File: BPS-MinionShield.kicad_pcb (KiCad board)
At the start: 2 copper layers, 85 x 66 mm, 83 parts, among them J1 TempConn1, J2 TempConn2, J3 Conn_01x24_Female

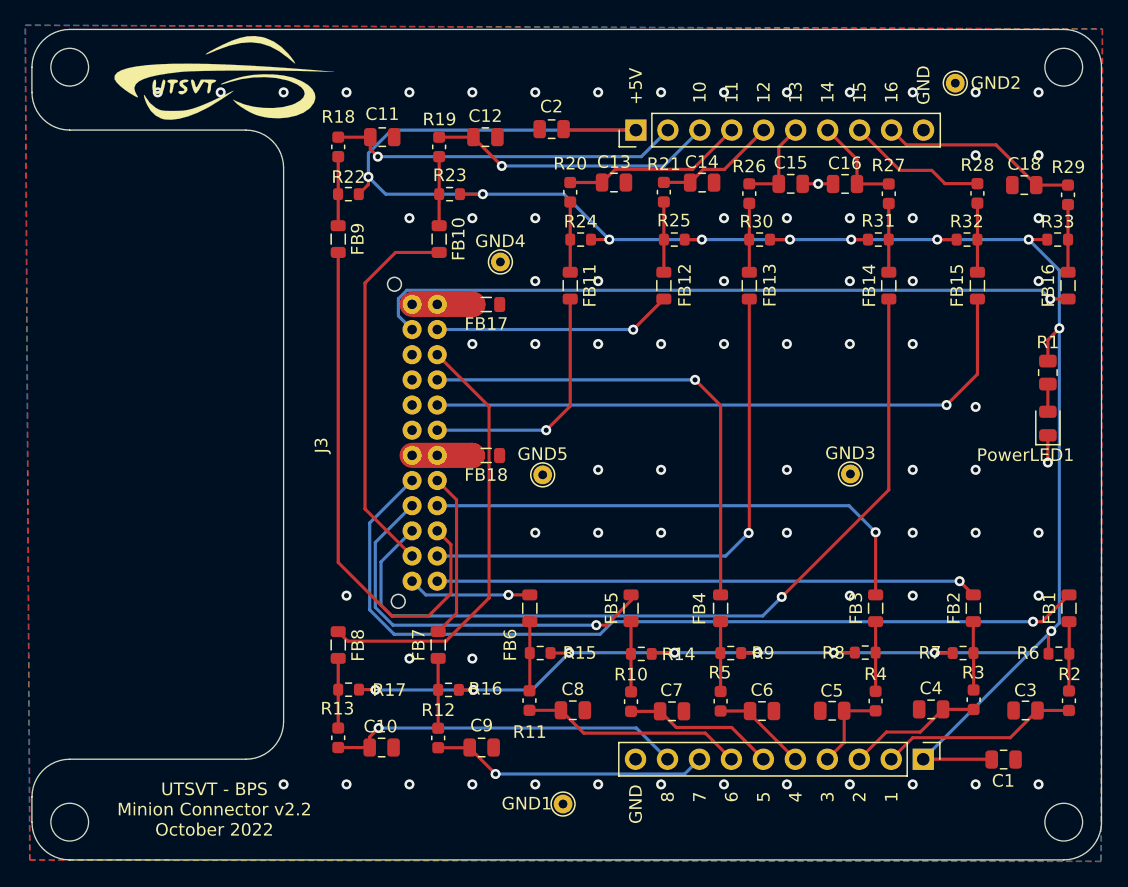
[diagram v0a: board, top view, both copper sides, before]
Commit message: removed some gnd test points
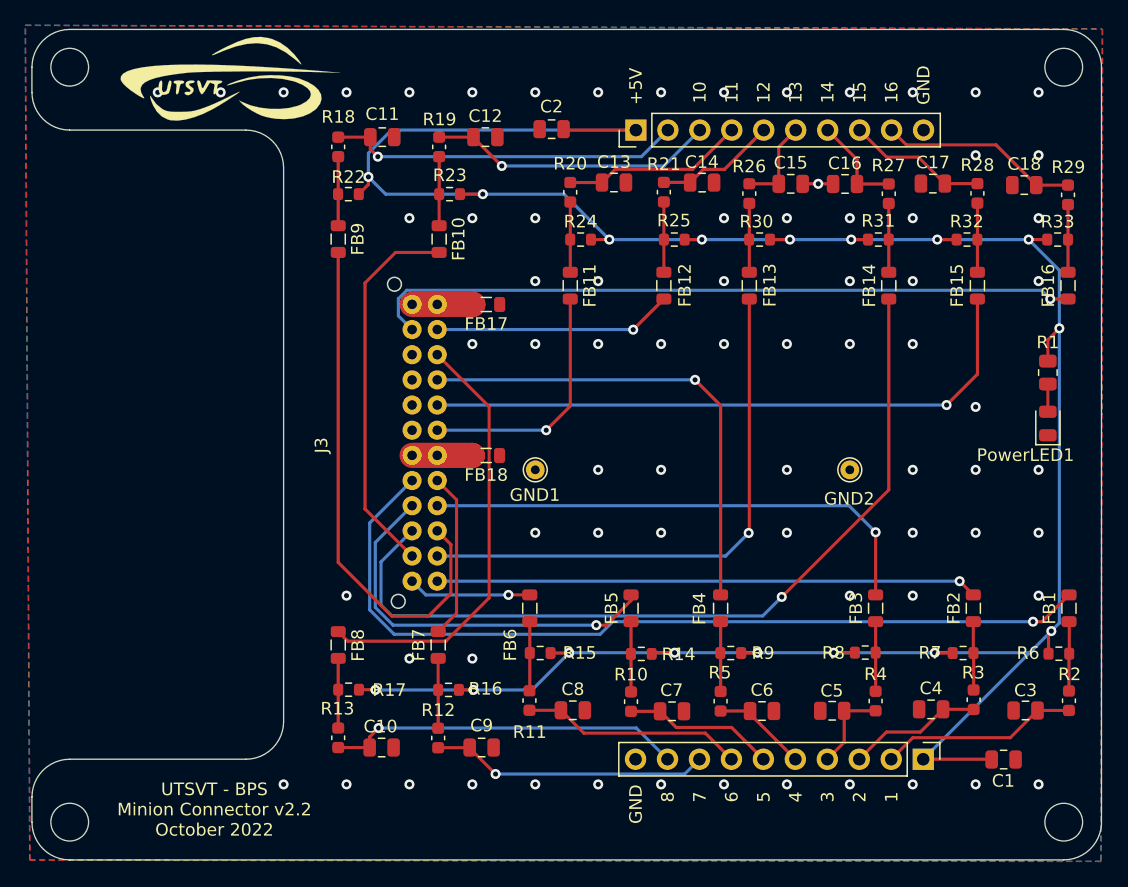
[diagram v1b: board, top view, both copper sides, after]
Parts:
- removed GND3, GND4, GND5: TestPoint, TestPoint:TestPoint_THTPad_D1.5mm_Drill0.7mm
- added C17: 1u, Capacitor_SMD:C_0805_2012Metric, F.Cu at (171.6, 82.2)
- moved GND2 31.9 mm to (165.0, 105.0), turned to 180 degrees
- moved GND1 26.7 mm to (140.0, 105.0), turned to 90 degrees
- moved G*** 0.49 mm to (127.9, 125.6)
- moved G*** 0.49 mm to (115.5, 74.1)
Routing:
- net GND: track 5.04 -> 2.88 mm

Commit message: implemented hannah changes and added personalization
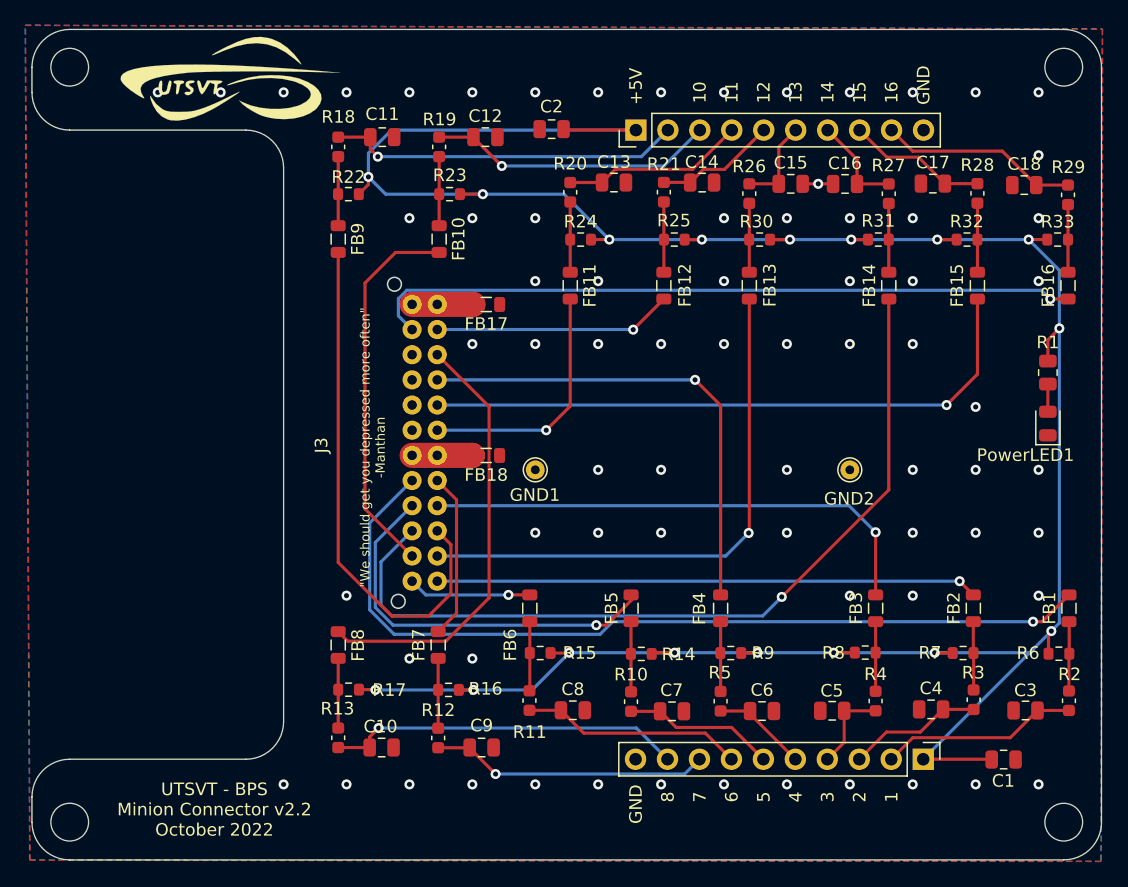
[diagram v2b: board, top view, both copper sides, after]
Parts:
- added G***: LOGO, LOGO, B.Cu at (156.2, 108.0)
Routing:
- net GND: vias 73 -> 72
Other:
- board text added: "{dblquote}We should get you depressed more often{dblquote} -Manthan"
- board text added: "{dblquote}You spent $10 on that haircut just to get no bitches?{dblquote} Tasnia Bari to Raymond Jiang"

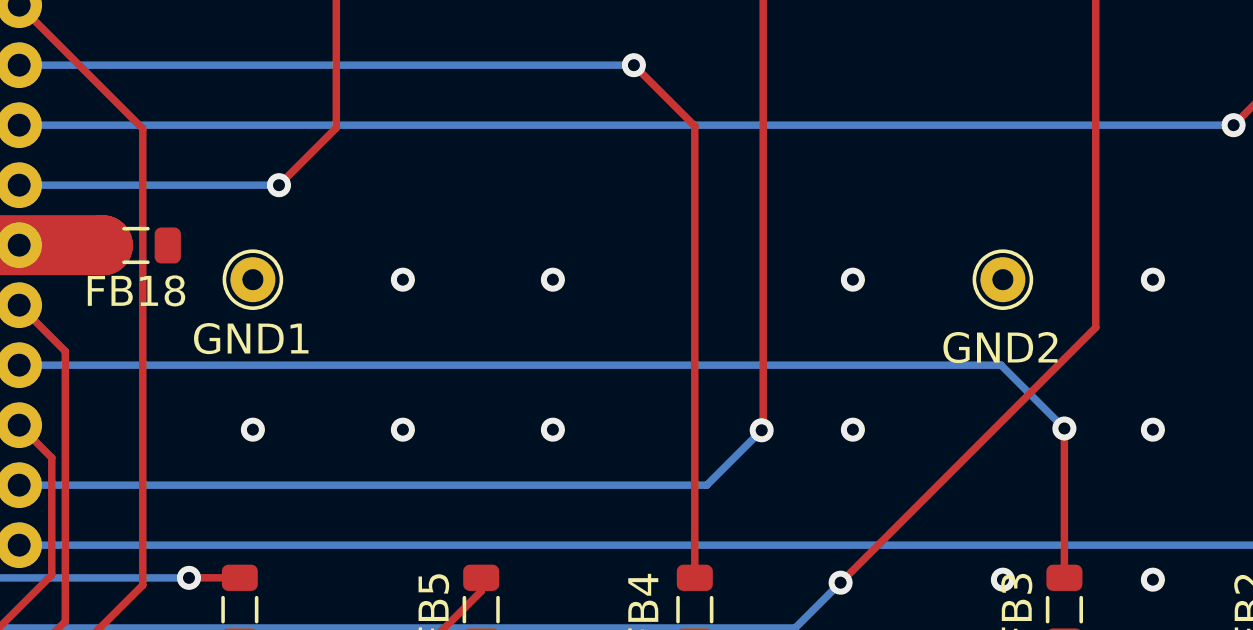
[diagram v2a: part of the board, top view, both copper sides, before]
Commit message: keep just 1 gnd testpoint
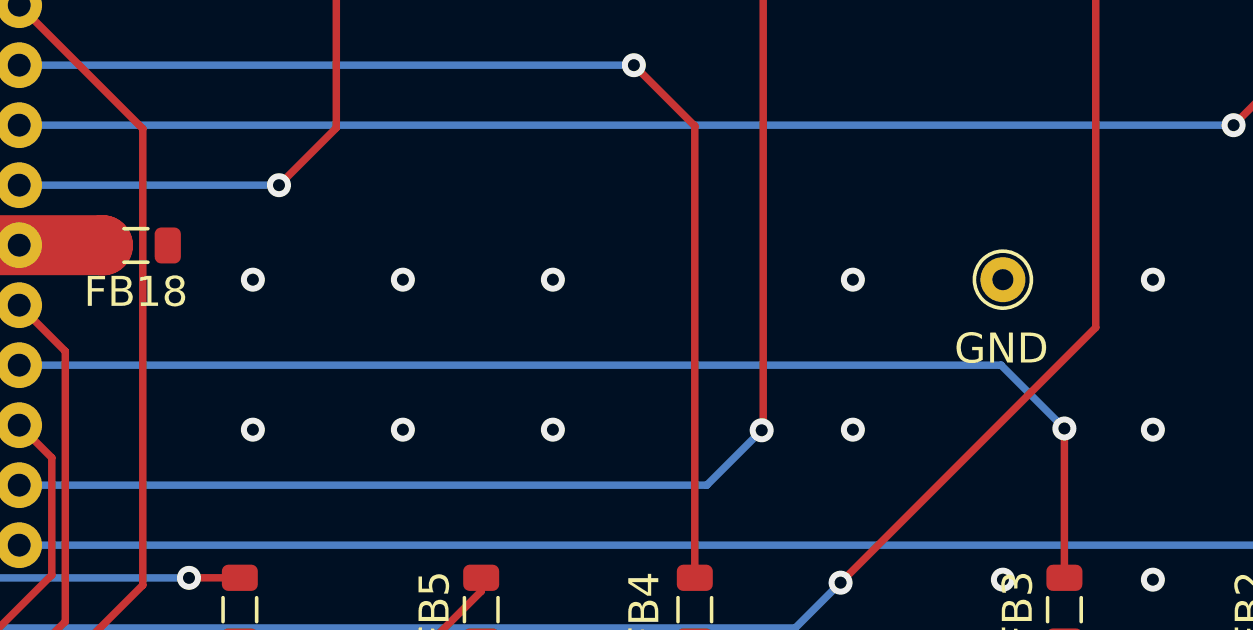
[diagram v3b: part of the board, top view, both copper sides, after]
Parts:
- removed GND1: TestPoint, TestPoint:TestPoint_THTPad_D1.5mm_Drill0.7mm
- renumbered GND2 to GND
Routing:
- net GND: vias 72 -> 73
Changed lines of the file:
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@@
     (property "Sheetname" "")
     (attr exclude_from_pos_files)
-    (fp_text reference "GND2" (at 0.05 -2.3 180) (layer "F.SilkS")
+    (fp_text reference "GND" (at 0.05 -2.3 180) (layer "F.SilkS")
       (effects (font (size 1 1) (thickness 0.15)))
     )
@@
     )
   )
-  (footprint "TestPoint:TestPoint_THTPad_D1.5mm_Drill0.7mm" (layer "F.Cu")
-    (at 140 105 90)
-    (descr "THT pad as test Point, diameter 1.5mm, hole diameter 0.7mm")
-    (tags "test point THT pad")
-    (property "Sheetfile" "BPS-MinionShield.kicad_sch")
-    (property "Sheetname" "")
-    (attr exclude_from_pos_files)
-    (fp_text reference "GND1" (at -2 -0.03 180) (layer "F.SilkS")
-      (effects (font (size 1 1) (thickness 0.15)))
-    )
-    (fp_text value "TestPoint" (at 0 1.75 90) (layer "F.Fab")
-      (effects (font (size 1 1) (thickness 0.15)))
-    )
-    (fp_text user "${REFERENCE}" (at 0 -1.65 90) (layer "F.Fab")
-      (effects (font (size 1 1) (thickness 0.15)))
-    )
-    (fp_circle (center 0 0) (end 0 0.95) (layer "F.SilkS") (width 0.12) (fill none))
-    (fp_circle (center 0 0) (end 1.25 0) (layer "F.CrtYd") (width 0.05) (fill none))
-    (pad "1" thru_hole circle (at 0 0 90) (size 1.5 1.5) (drill 0.7) (layers *.Cu *.Mask)
-      (net 2 "GND") (pinfunction "1") (pintype "passive"))
-  )
   (footprint "Capacitor_SMD:C_0805_2012Metric" (layer "F.Cu")
     (at 171.46 124.035)
@@
   (via (at 170 105) (size 0.8) (drill 0.4) (layers "F.Cu" "B.Cu") (free) (net 2))
   (via (at 140 90) (size 0.8) (drill 0.4) (layers "F.Cu" "B.Cu") (free) (net 2))
+  (via (at 140 105) (size 0.8) (drill 0.4) (layers "F.Cu" "B.Cu") (free) (net 2))
   (via (at 175 105) (size 0.8) (drill 0.4) (layers "F.Cu" "B.Cu") (free) (net 2))
   (via (at 145 110) (size 0.8) (drill 0.4) (layers "F.Cu" "B.Cu") (free) (net 2))

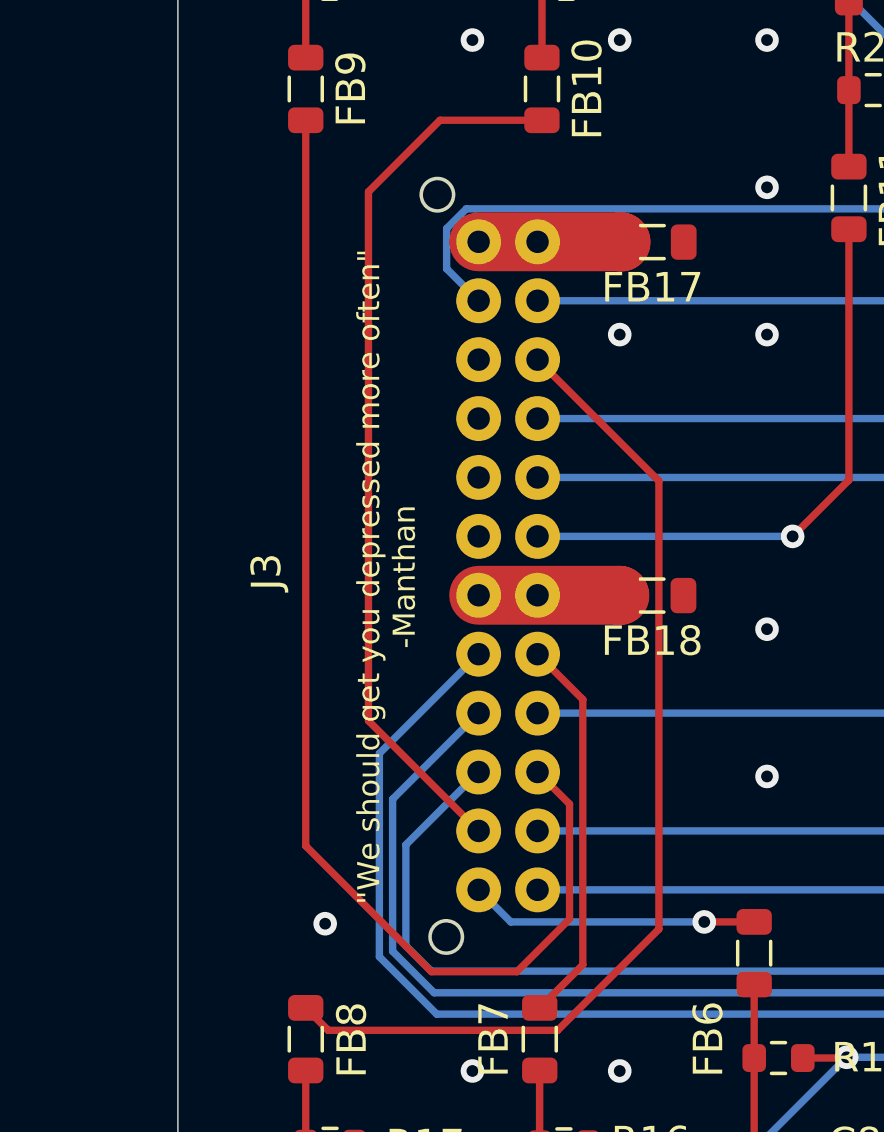
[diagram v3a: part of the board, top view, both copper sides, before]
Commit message: fix connector footprint, change quotes
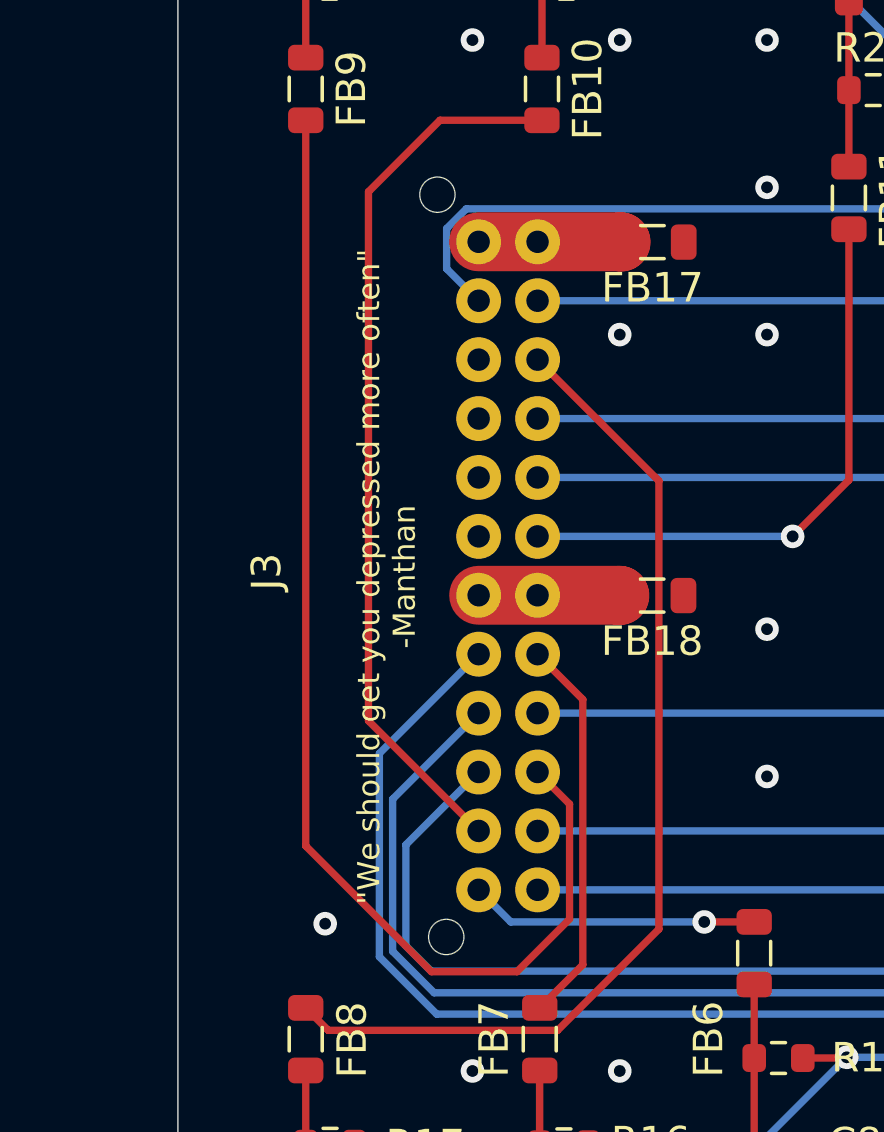
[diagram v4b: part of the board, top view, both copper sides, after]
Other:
- board text added: "Champers was here"
- board text added: "{dblquote}Too much lube is never a problem{dblquote} -Raymond Jiang"
- board text added: "{dblquote}git gud{dblquote} -Prof. Alex Hanson to 302 students during a midterm"
- board text removed: "Why you turn me over???"
- board text removed: "{dblquote}You spent $10 on that haircut just to get no bitches?{dblquote} Tasnia Bari to Raymond Jiang"
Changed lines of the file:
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@@
       (effects (font (size 1 1) (thickness 0.15)))
     )
-    (fp_circle (center 23.6 -1.4) (end 23.05 -1.4) (layer "Edge.Cuts") (width 0.12) (fill none))
-    (fp_circle (center -1.6 -1.1) (end -2.15 -1.1) (layer "Edge.Cuts") (width 0.12) (fill none))
     (fp_line (start -2 3) (end 24 3) (layer "F.CrtYd") (width 0.05))
     (fp_line (start 24 -10.2) (end 24 3) (layer "F.CrtYd") (width 0.05))
-    (fp_line (start -2 3) (end -2 -10.2) (layer "F.CrtYd") (width 0.05))
     (fp_line (start -2 -10.2) (end 24 -10.2) (layer "F.CrtYd") (width 0.05))
+    (fp_line (start -2 3) (end -2 -10.2) (layer "F.CrtYd") (width 0.05))
+    (pad "" np_thru_hole circle (at 23.6 -1.4 90) (size 1.2 1.2) (drill 1.2) (layers F&B.Cu *.Mask))
+    (pad "" np_thru_hole circle (at -1.6 -1.1 90) (size 1.2 1.2) (drill 1.2) (layers F&B.Cu *.Mask))
     (pad "1" thru_hole circle (at 22 2 90) (size 1.524 1.524) (drill 0.762) (layers *.Cu *.Mask)
       (net 56 "Net-(FB17-Pad2)") (pinfunction "Pin_1") (pintype "passive"))
@@
   (gr_arc (start 117 78) (mid 119.12132 78.87868) (end 120 81) (layer "Edge.Cuts") (width 0.05))
   (gr_arc (start 185 133.15) (mid 184.068967 135.173912) (end 182 136) (layer "Edge.Cuts") (width 0.05))
-  (gr_text "{dblquote}You spent $10 on that haircut just to get no bitches?{dblquote} \nTasnia Bari to Raymond Jiang" (at 160.68 123.58) (layer "B.SilkS")
+  (gr_text "{dblquote}Too much lube is never a problem{dblquote}\n-Raymond Jiang" (at 155 123.58) (layer "B.SilkS")
     (effects (font (size 0.75 0.75) (thickness 0.15)) (justify mirror))
   )
-  (gr_text "Why you turn me over???" (at 115.44 75.57) (layer "B.SilkS")
-    (effects (font (size 1 1) (thickness 0.15)) (justify mirror))
+  (gr_text "{dblquote}git gud{dblquote}\n-Prof. Alex Hanson to 302 students during a midterm" (at 150 75) (layer "B.SilkS")
+    (effects (font (size 1 1) (thickness 0.15)) (justify left mirror))
+  )
+  (gr_text "Champers was here" (at 125 103 -90) (layer "B.SilkS")
+    (effects (font (size 0.75 0.75) (thickness 0.16)) (justify mirror))
   )
   (gr_text "Dr. Gary Hallock" (at 127 134) (layer "B.SilkS")
